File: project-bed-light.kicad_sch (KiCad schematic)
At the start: 0 parts

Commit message: Create schematic
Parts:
- added J1: 2060-452_998-404, WAGO_2060-452-998-404:WAGO_2060-452_998-404, symbol 2060-452_998-404:2060-452_998-404
- added S1: B3FS-1010P, B3FS-1010:SW_B3FS-1010P, symbol B3FS-1010P:B3FS-1010P
- added U2: Pink Panda v2.1.0, symbol pink_panda:pink_panda_v2.1.0
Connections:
- new net: S1.2, U2.3 (P0.04)
- new net GND: J1.2_1 (2), J1.2_2 (2), S1.1, U2.25 (GND)
- new net Reverse Polarity Protection/IN: J1.1_1 (1), J1.1_2 (1)
- new net VDD: U2.12 (VDD_OUT)
- no-connect marks 0 -> 25
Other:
- added sheet Reverse Polarity Protection (reverse_polarity_protection.kicad_sch)
- added sheet TPS6293x Converter (tps6293x_converter.kicad_sch)

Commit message: sch: first draft
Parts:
- added J2: WAGO_2060-453-998-404, Connector_Wire-to-Board:WAGO_2060-453-998-404, symbol WAGO_2060-453-998-404:WAGO_2060-453-998-404
- added U3: ~, SO:TSSOP-14_4.4x5mm_P0.65mm, symbol TI_TXU0104PWR:TXU0104PWR
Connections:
- net GND: now also J2.3_1 (3), J2.3_2 (3), U3.7 (GND)
- net at U2.13 (P0.20): now also U3.2 (A1)
- net +3.3V: now reaches U2.27 (VDD_OUT)
- net +3.3V: now also U3.1 (V_{CCA}), U3.8 (OE)
- net Reverse Polarity Protection/IN renamed +24V
- net +24V: now also J2.1_1 (1), J2.1_2 (1)
- net VDD renamed +5V
- net +5V: now also U3.14 (V_{CCB})
- new net D_{IN}: J2.2_1 (2), J2.2_2 (2), U3.13 (B1Y)
- no-connect marks 25 -> 29
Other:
- moved on the sheet: S1, U2

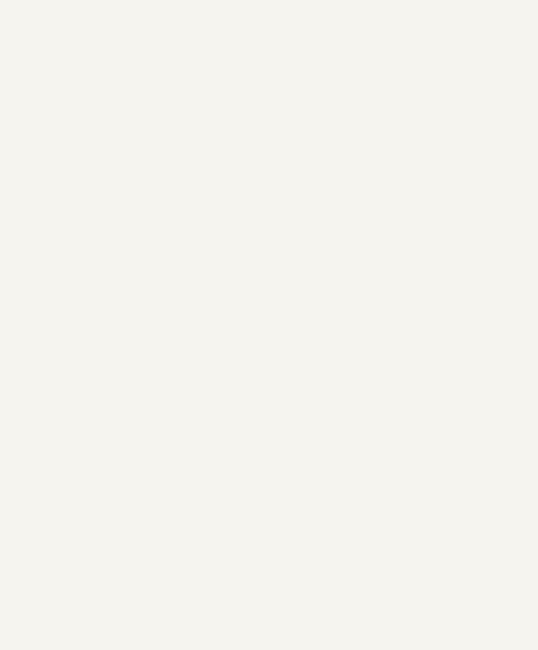
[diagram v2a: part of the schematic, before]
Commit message: sch: add mounting holes
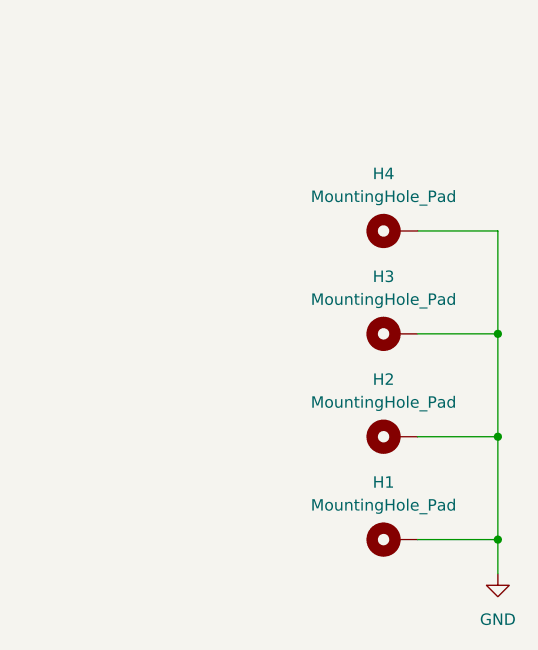
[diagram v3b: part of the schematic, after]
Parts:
- added H1, H2, H3, H4: MountingHole_Pad, MountingHole:MountingHole_2.7mm_M2.5_ISO7380_Pad, symbol Mechanical:MountingHole_Pad
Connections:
- net GND: now also H1.1, H2.1, H3.1, H4.1

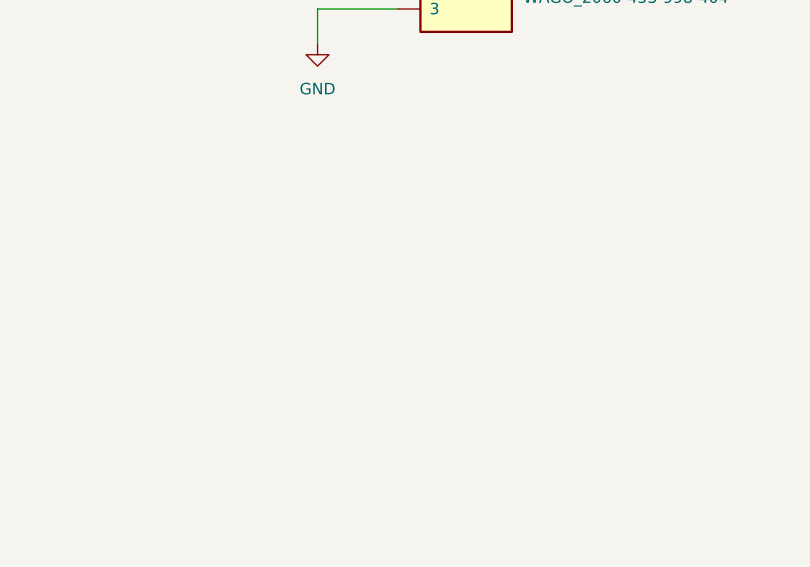
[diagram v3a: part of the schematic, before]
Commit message: sch: add power header
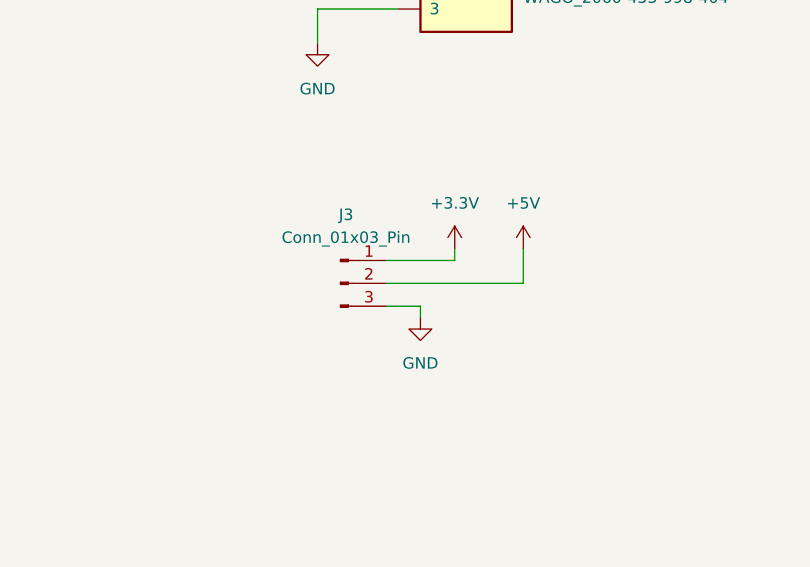
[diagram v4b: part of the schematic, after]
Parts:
- added J3: Conn_01x03_Pin, symbol Connector:Conn_01x03_Pin
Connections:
- net +3.3V: now also J3.1 (Pin_1)
- net +5V: now also J3.2 (Pin_2)
- net GND: now also J3.3 (Pin_3)

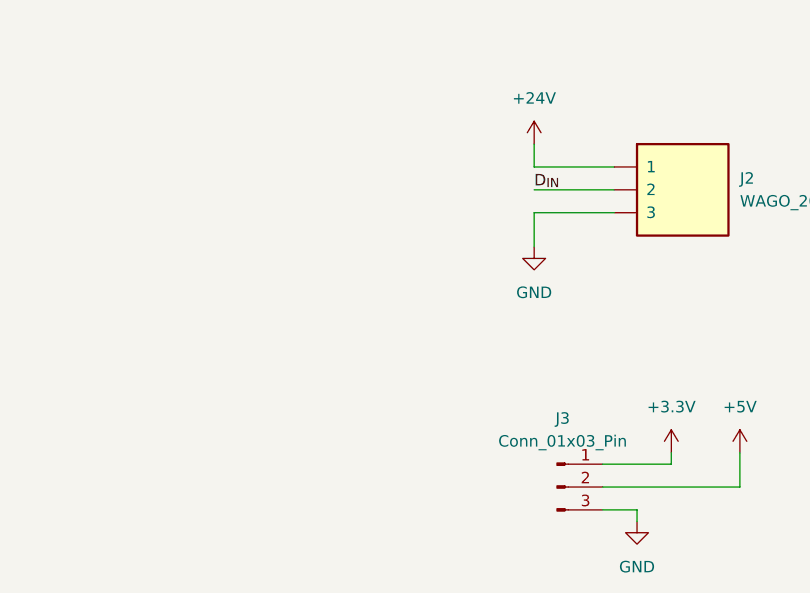
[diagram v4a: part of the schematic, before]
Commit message: sch: add 24V cap
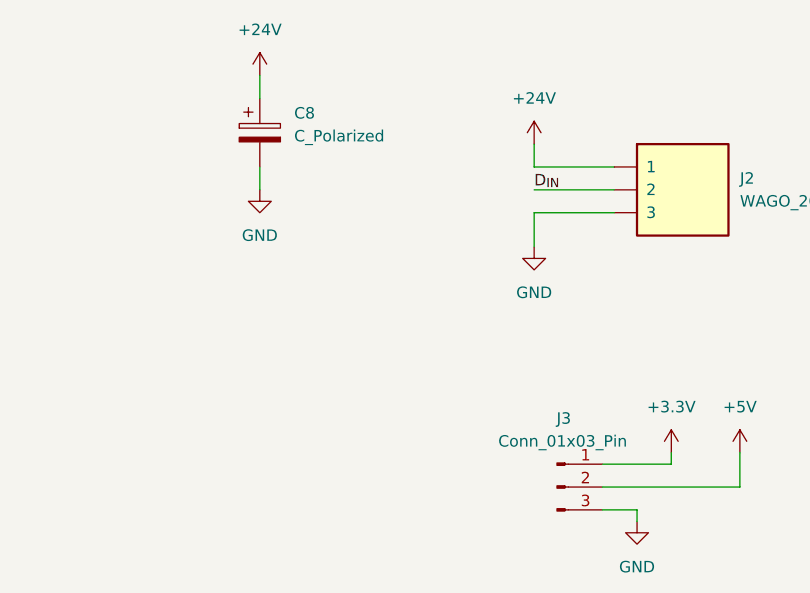
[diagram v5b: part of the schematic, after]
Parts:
- added C8: C_Polarized, symbol Device:C_Polarized
- J3: footprint (none) -> Connector_PinHeader_2.54mm:PinHeader_1x03_P2.54mm_Vertical
- U2: footprint (none) -> pink_panda:pink_panda_SMD
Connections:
- net +24V: now also C8.1
- net GND: now also C8.2
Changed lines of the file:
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@@
+	(wire
+		(pts
+			(xy 182.88 27.94) (xy 182.88 30.48)
+		)
+		(stroke
+			(width 0)
+			(type default)
+		)
+	)
 	(wire
 		(pts
@@
 		(pts
 			(xy 46.99 87.63) (xy 55.88 87.63)
+		)
+		(stroke
+			(width 0)
+			(type default)
+		)
+	)
+	(wire
+		(pts
+			(xy 182.88 38.1) (xy 182.88 40.64)
 		)
 		(stroke
@@
 	)
 	(symbol
+		(lib_id "Device:C_Polarized")
+		(at 182.88 34.29 0)
+		(unit 1)
+		(exclude_from_sim no)
+		(in_bom yes)
+		(on_board yes)
+		(dnp no)
+		(fields_autoplaced yes)
+		(property "Reference" "C8"
+			(at 186.69 32.1309 0)
+			(effects
+				(font
+					(size 1.27 1.27)
+				)
+				(justify left)
+			)
+		)
+		(property "Value" "C_Polarized"
+			(at 186.69 34.6709 0)
+			(effects
+				(font
+					(size 1.27 1.27)
+				)
+				(justify left)
+			)
+		)
+		(property "Footprint" ""
+			(at 183.8452 38.1 0)
+			(effects
+				(font
+					(size 1.27 1.27)
+				)
+				(hide yes)
+			)
+		)
+		(property "Datasheet" "~"
+			(at 182.88 34.29 0)
+			(effects
+				(font
+					(size 1.27 1.27)
+				)
+				(hide yes)
+			)
+		)
+		(property "Description" "Polarized capacitor"
+			(at 182.88 34.29 0)
+			(effects
+				(font
+					(size 1.27 1.27)
+				)
+				(hide yes)
+			)
+		)
+		(pin "2"
+		)
+		(pin "1"
+		)
+		(instances
+			(project ""
+				(path "/86193608-8b37-4e1b-8d51-bc4738e07deb"
+					(reference "C8")
+					(unit 1)
+				)
+			)
+		)
+	)
+	(symbol
 		(lib_id "Connector:Conn_01x03_Pin")
 		(at 215.9 73.66 0)
@@
 		(on_board yes)
 		(dnp no)
-		(fields_autoplaced yes)
 		(property "Reference" "J3"
-			(at 216.535 66.04 0)
+			(at 216.662 66.04 0)
 			(effects
 				(font
@@
 			)
 		)
-		(property "Footprint" ""
+		(property "Footprint" "Connector_PinHeader_2.54mm:PinHeader_1x03_P2.54mm_Vertical"
 			(at 215.9 73.66 0)
 			(effects
@@
 				(path "/86193608-8b37-4e1b-8d51-bc4738e07deb"
 					(reference "S1")
+					(unit 1)
+				)
+			)
+		)
+	)
+	(symbol
+		(lib_id "power:+24V")
+		(at 182.88 27.94 0)
+		(unit 1)
+		(exclude_from_sim no)
+		(in_bom yes)
+		(on_board yes)
+		(dnp no)
+		(fields_autoplaced yes)
+		(property "Reference" "#PWR019"
+			(at 182.88 31.75 0)
+			(effects
+				(font
+					(size 1.27 1.27)
+				)
+				(hide yes)
+			)
+		)
+		(property "Value" "+24V"
+			(at 182.88 22.86 0)
+			(effects
+				(font
+					(size 1.27 1.27)
+				)
+			)
+		)
+		(property "Footprint" ""
+			(at 182.88 27.94 0)
+			(effects
+				(font
+					(size 1.27 1.27)
+				)
+				(hide yes)
+			)
+		)
+		(property "Datasheet" ""
+			(at 182.88 27.94 0)
+			(effects
+				(font
+					(size 1.27 1.27)
+				)
+				(hide yes)
+			)
+		)
+		(property "Description" "Power symbol creates a global label with name \"+24V\""
+			(at 182.88 27.94 0)
+			(effects
+				(font
+					(size 1.27 1.27)
+				)
+				(hide yes)
+			)
+		)
+		(pin "1"
+		)
+		(instances
+			(project "project-bed-light"
+				(path "/86193608-8b37-4e1b-8d51-bc4738e07deb"
+					(reference "#PWR019")
 					(unit 1)
 				)
@@
 			)
 		)
-		(property "Footprint" ""
+		(property "Footprint" "pink_panda:pink_panda_SMD"
 			(at 71.12 88.9 0)
 			(effects
@@
 					(unit 1)
 				)
+			)
+		)
+	)
+	(symbol
+		(lib_id "power:GND")
+		(at 182.88 40.64 0)
+		(unit 1)
+		(exclude_from_sim no)
+		(in_bom yes)
+		(on_board yes)
+		(dnp no)
+		(fields_autoplaced yes)
+		(property "Reference" "#PWR020"
+			(at 182.88 46.99 0)
+			(effects
+				(font
+					(size 1.27 1.27)
+				)
+				(hide yes)
+			)
+		)
+		(property "Value" "GND"
+			(at 182.88 45.72 0)
+			(effects
+				(font
+					(size 1.27 1.27)
+				)
+			)
+		)
+		(property "Footprint" ""
+			(at 182.88 40.64 0)
+			(effects
+				(font
+					(size 1.27 1.27)
+				)
+				(hide yes)
+			)
+		)
+		(property "Datasheet" ""
+			(at 182.88 40.64 0)
+			(effects
+				(font
+					(size 1.27 1.27)
+				)
+				(hide yes)
+			)
+		)
+		(property "Description" "Power symbol creates a global label with name \"GND\" , ground"
+			(at 182.88 40.64 0)
+			(effects
+				(font
+					(size 1.27 1.27)
+				)
+				(hide yes)
+			)
+		)
+		(pin "1"
+		)
+		(instances
+			(project "project-bed-light"
+				(path "/86193608-8b37-4e1b-8d51-bc4738e07deb"
+					(reference "#PWR020")
+					(unit 1)
+				)

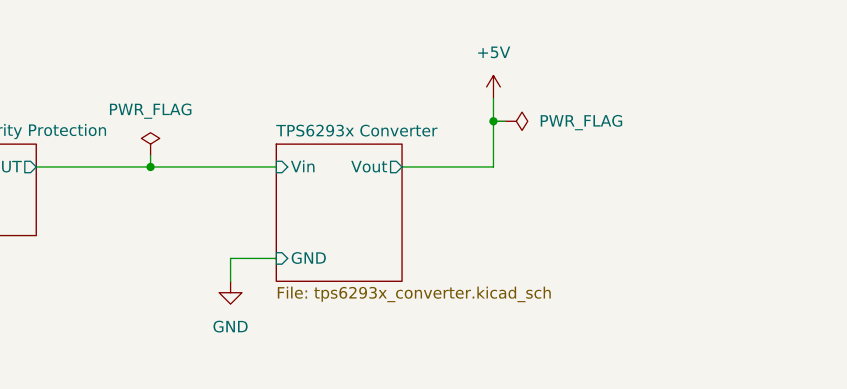
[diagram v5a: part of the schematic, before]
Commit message: pcb: first placement
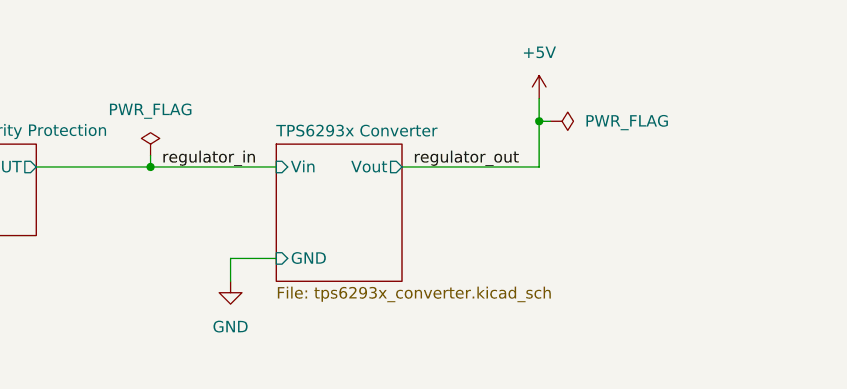
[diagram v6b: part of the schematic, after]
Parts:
- C8: footprint (none) -> Capacitor_SMD:CP_Elec_10x10
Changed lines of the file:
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@@
 	)
 	(junction
-		(at 139.7 33.02)
+		(at 144.78 33.02)
 		(diameter 0)
 		(color 0 0 0 0)
@@
 	(wire
 		(pts
-			(xy 139.7 33.02) (xy 139.7 30.48)
+			(xy 144.78 33.02) (xy 144.78 30.48)
 		)
 		(stroke
@@
 	(wire
 		(pts
-			(xy 139.7 38.1) (xy 139.7 33.02)
-		)
-		(stroke
-			(width 0)
-			(type default)
-		)
-	)
-	(wire
-		(pts
-			(xy 129.54 38.1) (xy 139.7 38.1)
+			(xy 144.78 38.1) (xy 144.78 33.02)
+		)
+		(stroke
+			(width 0)
+			(type default)
+		)
+	)
+	(wire
+		(pts
+			(xy 129.54 38.1) (xy 144.78 38.1)
 		)
 		(stroke
@@
 	(wire
 		(pts
-			(xy 139.7 33.02) (xy 140.97 33.02)
+			(xy 144.78 33.02) (xy 146.05 33.02)
 		)
 		(stroke
@@
 			(width 0)
 			(type default)
+		)
+	)
+	(label "regulator_out"
+		(at 130.81 38.1 0)
+		(effects
+			(font
+				(size 1.27 1.27)
+			)
+			(justify left bottom)
 		)
 	)
@@
 		)
 	)
+	(label "regulator_in"
+		(at 102.87 38.1 0)
+		(effects
+			(font
+				(size 1.27 1.27)
+			)
+			(justify left bottom)
+		)
+	)
 	(label "D_{IN}"
 		(at 142.24 102.87 180)
@@
 	(symbol
 		(lib_id "power:PWR_FLAG")
-		(at 140.97 33.02 270)
+		(at 146.05 33.02 270)
 		(unit 1)
 		(exclude_from_sim no)
@@
 		(fields_autoplaced yes)
 		(property "Reference" "#FLG03"
-			(at 142.875 33.02 0)
+			(at 147.955 33.02 0)
 			(effects
 				(font
@@
 		)
 		(property "Value" "PWR_FLAG"
-			(at 144.78 33.0199 90)
+			(at 149.86 33.0199 90)
 			(effects
 				(font
@@
 		)
 		(property "Footprint" ""
-			(at 140.97 33.02 0)
+			(at 146.05 33.02 0)
 			(effects
 				(font
@@
 		)
 		(property "Datasheet" "~"
-			(at 140.97 33.02 0)
+			(at 146.05 33.02 0)
 			(effects
 				(font
@@
 		)
 		(property "Description" "Special symbol for telling ERC where power comes from"
-			(at 140.97 33.02 0)
+			(at 146.05 33.02 0)
 			(effects
 				(font
@@
 			)
 		)
-		(property "Footprint" ""
+		(property "Footprint" "Capacitor_SMD:CP_Elec_10x10"
 			(at 183.8452 38.1 0)
 			(effects
@@
 	(symbol
 		(lib_id "power:+5V")
-		(at 139.7 30.48 0)
+		(at 144.78 30.48 0)
 		(unit 1)
 		(exclude_from_sim no)
@@
 		(fields_autoplaced yes)
 		(property "Reference" "#PWR013"
-			(at 139.7 34.29 0)
+			(at 144.78 34.29 0)
 			(effects
 				(font
@@
 		)
 		(property "Value" "+5V"
-			(at 139.7 25.4 0)
+			(at 144.78 25.4 0)
 			(effects
 				(font
@@
 		)
 		(property "Footprint" ""
-			(at 139.7 30.48 0)
+			(at 144.78 30.48 0)
 			(effects
 				(font
@@
 		)
 		(property "Datasheet" ""
-			(at 139.7 30.48 0)
+			(at 144.78 30.48 0)
 			(effects
 				(font
@@
 		)
 		(property "Description" "Power symbol creates a global label with name \"+5V\""
-			(at 139.7 30.48 0)
-			(effects
-				(font
+			(at 144.78 30.48 0)
+			(effects
+				(font
